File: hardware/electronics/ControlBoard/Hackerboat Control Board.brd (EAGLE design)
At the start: 177.8 x 114.3 mm, 52 parts, among them J3 3-1437664-0, U14 TPS54331, U15 TPS54331

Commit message: Everything in except the 15V boost converter and a couple of connectors
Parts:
- removed 5V/1-STAT: (no value), adafruit:CHIPLED_0805
- added 5V-STAT: (no value), adafruit:CHIPLED_0805
- added ACC_POWER: (no value), pinhead-1:2X08
- added BBB_CONSOLE: FTDI_BASICPTH, SparkFun-Connectors:FTDI_BASIC
- added C1, C2, C3, C4, C5, C6: (no value), resistor:C0603
- added C10, C11, C12, C13, C14, C15, C16, C35, C36, C37, C38, C39, C7, C8, C9: 100n, resistor:C0603
- added D1, D10, D11, D12, D13, D14, D15, D16, D17, D18, D19, D2, D3, D4, D5, D6, D7, D8, D9: (no value), adafruit:SOD-123
- added IC1: 74AHC1G08DBV, 74xx-little-us:SOT23-5
- added J1, J2: (no value), SparkFun-Connectors:1X03_LOCK
- added J4: (no value), SparkFun-Connectors:1X05_LOCK
- added J5: (no value), SparkFun-Connectors:1X09_LOCK
- added J6: (no value), SparkFun-Connectors:1X10_LOCK
- added J7: (no value), SparkFun-Connectors:1X18
- added MOTOR-CTRL-RELAYS: (no value), SparkFun-Connectors:DB9
- added POE-DEVICE, POE-LAN: RJ45, SparkFun-Connectors:RJ45-8
- added POWER_INPUT: 3-1437664-0, logos-headers:CONN-2
- added POWER_MONITOR: (no value), pinhead-1:2X06
- added POWER_STATE: HEADER_POS5_70555, con-molex-c-grid-sl:70555-POS5
- added R1, R13, R14, R15, R2, R25, R29, R3, R30, R34, R35, R36, R42, R43, R44, R48, R69, R7, R70, R71, R75, R76, R77, R8, R81, R82, R83, R9: 10K, resistor:R0603
- added R10, R16, R31, R37, R4, R45, R72, R78, R84: 100K, resistor:R0603
- added R11, R17, R32, R40, R46, R5, R55, R73, R79, R85: 0R05, resistor:R2512
- added R12, R18, R33, R41, R47, R56, R6, R74, R80, R86: 33K, resistor:R0603
- added R49, R50: (no value), resistor:R0603
- added R51, R52, R53, R54: 4u7, resistor:R0603
- added S1: FONA, adafruit-sensor-boards:FONA-3G
- added SERIAL_CONSOLE: HEADER_POS4_70555, con-molex-c-grid-sl:70555-POS4
- added STATUS_LIGHTS, STEERING: HEADER_POS3_70555, con-molex-c-grid-sl:70555-POS3
- added U1, U11, U2, U20, U22, U24, U4, U6, U8: IPS6041G, hackerbot:SO08
- added U10, U12, U21, U23, U25, U27, U3, U5, U7, U9: INA169, logos-power:SOT23-5L
- added U13, U16, U17: (no value), adafruit:TSSOP20
- added U18, U19: ADC128D818, ti-stuff:TSSOP16
- added U26: (no value), adafruit:VFSOP-8
- J3: value 3-1437664-0 -> (none); device logos-headers:CONN-2 -> SparkFun-Connectors:1X04_LOCK
- moved J3 501.0 mm to (19.7, -398.1), turned to 0 degrees
- moved C17 406.4 mm to (429.3, 31.8)
- moved C18 406.4 mm to (429.3, 28.6)
- moved C19 406.4 mm to (429.3, 26.0)
- moved C20 406.4 mm to (433.7, 25.4)
- moved C21 406.4 mm to (442.6, 35.6)
- moved C22 406.4 mm to (437.5, 25.4)
- moved C23 406.4 mm to (439.4, 25.4)
- moved C24 406.4 mm to (452.1, 22.2)
- moved C25 406.4 mm to (445.1, 22.2)
- moved D35 406.4 mm to (442.6, 30.5)
- moved L1 406.4 mm to (448.3, 30.5)
- moved R21 406.4 mm to (435.6, 25.4)
- moved R22 406.4 mm to (443.2, 25.4)
- moved R23 406.4 mm to (441.3, 25.4)
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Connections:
- net N$109 renamed BBB_MISO
- net N$168 renamed BBB_SCLK
- net N$169 renamed BBB_MOSI
- net RX1 renamed N$21
- net TX1 renamed BBB_STAT_LIGHT_3V3
- removed net 7V4: C26.1, C27.1, L2.2, R27.2, R39.2
- removed net N$105: U$1.86, U$2.6
- removed net N$111: U$1.66, U$2.16
- removed net N$112: U$1.64, U$2.17
- removed net N$113: U$1.62, U$2.18
- removed net N$114: U$1.60, U$2.19
- removed net N$115: U$1.58, U$2.20
- removed net N$116: U$1.56, U$2.21
- removed net N$122: U$1.40, U$3.5
- removed net N$123: U$1.38, U$3.6
- removed net N$124: U$1.36, U$3.7
- removed net N$125: U$1.34, U$3.8
- removed net N$126: U$1.32, U$3.9
- removed net N$127: U$1.30, U$3.10
- removed net N$128: U$1.28, U$3.11
- removed net N$129: U$1.26, U$3.12
- removed net N$130: U$1.24, U$3.13
- removed net N$131: U$1.22, U$3.14
- removed net N$132: U$1.20, U$3.15
- removed net N$133: U$1.18, U$3.16
- removed net N$134: U$1.16, U$3.17
- removed net N$135: U$1.14, U$3.18
- removed net N$136: U$1.12, U$3.19
- removed net N$137: U$1.10, U$3.20
- removed net N$138: U$1.8, U$3.21
- removed net N$139: U$1.6, U$3.22
- removed net N$140: U$1.4, U$3.23
- removed net N$145: U$1.37, U$4.6
- removed net N$147: U$1.33, U$4.8
- removed net N$148: U$1.31, U$4.9
- removed net N$149: U$1.29, U$4.10
- removed net N$150: U$1.27, U$4.11
- removed net N$151: U$1.25, U$4.12
- removed net N$152: U$1.23, U$4.13
- removed net N$153: U$1.21, U$4.14
- removed net N$154: U$1.19, U$4.15
- removed net N$155: U$1.17, U$4.16
- removed net N$156: U$1.15, U$4.17
- removed net N$157: U$1.13, U$4.18
- removed net N$158: U$1.11, U$4.19
- removed net N$159: U$1.9, U$4.20
- removed net N$160: U$1.7, U$4.21
- removed net N$161: U$1.5, U$4.22
- removed net N$162: U$1.3, U$4.23
- removed net N$173: U$1.65, U$5.16
- removed net N$174: U$1.63, U$5.17
- removed net N$175: U$1.61, U$5.18
- removed net N$196: IMU.SDA, R20.1
- removed net N$197: IMU.SCL, R19.1
- removed net RX0: U$1.70, U$2.14
- removed net SERVO_EN: U15.3
- removed net TX0: U$1.72, U$2.13
- new net +15V: ACC_POWER.13, ACC_POWER.14, POE-DEVICE.4, POE-DEVICE.5
- new net +7V4: ACC_POWER.15, ACC_POWER.16, J1.1, R55.2, STEERING.P$1, U27.4
- new net +7V4_OUT: C26.1, C27.1, L2.2, R27.2, R39.2, R55.1, U27.3
- new net AUX_ADC_0: POWER_MONITOR.10, U19.11
- new net AUX_ADC_1: POWER_MONITOR.11, U19.10
- new net AUX_GPIO_0_3V3: U$1.21, U$4.14, U16.9
- new net AUX_GPIO_0_5V: U16.12
- new net AUX_GPIO_1_3V3: U$1.23, U$4.13, U17.4
- new net AUX_GPIO_1_5V: U17.17
- new net AUX_GPIO_2_3V3: U$1.25, U$4.12, U17.5
- new net AUX_GPIO_2_5V: U17.16
- new net AUX_GPIO_3_3V3: U$1.27, U$4.11, U17.6
- new net AUX_GPIO_3_5V: U17.15
- new net AUX_GPIO_4_3V3: U$1.29, U$4.10, U17.7
- new net AUX_GPIO_4_5V: U17.14
- new net AUX_GPIO_5_3V3: U$1.33, U$4.8, U17.8
- new net AUX_GPIO_5_5V: U17.13
- new net BATMON: D13.C, R49.1, R50.2, U$1.86, U$2.6
- new net BBB_I2C_1_SCL: IMU.SCL, J6.4, R19.1, U$1.63, U$5.17
- new net BBB_I2C_1_SDA: IMU.SDA, J6.5, R20.1, U$1.64, U$2.17
- new net BBB_I2C_2_SCL: R53.1, U$1.65, U$5.16, U26.P$4
- new net BBB_I2C_2_SDA: R54.1, U$1.66, U$2.16, U26.P$5
- new net BBB_RESET_3V3: R48.2, U$1.56, U$2.21, U16.8
- new net BBB_RESET_5V: U16.13
- new net BBB_STATUS_LIGHTS_5V: J2.2, STATUS_LIGHTS.P$2
- new net BBB_STATUS_LIGHT_3V3: U16.7
- new net BBB_STATUS_LIGHT_5V: U16.14
- new net BBB_UART0_DTR: BBB_CONSOLE.DTR, J3.1, SERIAL_CONSOLE.P$1
- new net BBB_UART0_RX: BBB_CONSOLE.RXI, J3.2, SERIAL_CONSOLE.P$2
- new net BBB_UART0_TX: BBB_CONSOLE.TXO, J3.3, SERIAL_CONSOLE.P$3
- new net BBB_UART1_RX_3V3: U$1.70, U$2.14, U17.1
- new net BBB_UART1_RX_5V: U17.20
- new net BBB_UART1_TX_3V3: U$1.72, U$2.13, U17.3
- new net BBB_UART1_TX_5V: U17.18
- new net CELL_CTS: J7.9, S1.CTS, U$1.31, U$4.9
- new net CELL_KEY: J7.8, S1.KEY, U$1.40, U$3.5
- new net CELL_NET_STATUS: J7.5, S1.NS, U$1.34, U$3.8
- new net CELL_POWER_STATUS: J7.6, S1.PS, U$1.28, U$3.11
- new net CELL_RESET: J7.14, S1.RST, U$1.36, U$3.7
- new net CELL_RING: J7.7, S1.RI, U$1.30, U$3.10
- new net CELL_RTS: J7.11, S1.RTS, U$1.32, U$3.9
- new net CELL_RX: J7.13, S1.RX, U$1.37, U$4.6
- new net CELL_TX: J7.12, S1.TX, U$1.38, U$3.6
- new net CHARGE_CURRENT: POWER_MONITOR.7, U19.12
- new net CHARGE_VOLTAGE: POWER_MONITOR.6, U19.13
- new net DISARM_RELAY_IN_3V3: U$1.22, U$3.14, U16.6
- new net DISARM_RELAY_IN_5V: J4.2, POWER_STATE.P$2, U16.15
- new net ENABLE_RELAY_IN_3V3: U$1.20, U$3.15, U16.5
- new net ENABLE_RELAY_IN_5V: IC1.2, J4.1, POWER_STATE.P$1, U16.16
- new net GNSS_ENABLE: GPS.EN, J5.8, U$1.58, U$2.20
- new net GNSS_FIX: GPS.FIX, J5.6, U$1.61, U$5.18
- new net MOT_CURRENT: POWER_MONITOR.3, U19.15
- new net MOT_VOLTAGE: POWER_MONITOR.2, U19.14
- new net N$1: R1.2, R2.1, U1.3
- new net N$10: R25.2, R29.1, U6.3
- new net N$11: R30.2, U6.2
- new net N$12: R31.1, R32.1, U6.4, U7.3
- new net N$13: R34.2, R35.1, U8.3
- new net N$14: R36.2, U8.2
- new net N$15: R37.1, R40.1, U10.3, U8.4
- new net N$16: R42.2, R43.1, U11.3
- new net N$17: R44.2, U11.2
- new net N$18: R45.1, R46.1, U11.4, U12.3
- new net N$19: GPS.PPS, J5.1
- new net N$2: R3.2, U1.2
- new net N$20: GPS.VBAT, J5.7
- new net N$23: R52.1, U18.2, U19.2, U26.P$8
- new net N$24: R69.2, R70.1, U20.3
- new net N$25: R71.2, U20.2
- new net N$26: R72.1, R73.1, U20.4, U21.3
- new net N$27: R51.1, U18.3, U19.3, U26.P$1
- new net N$28: IMU.3VO, J6.2
- new net N$29: IMU.GINT, J6.6
- new net N$3: R4.1, R5.1, U1.4, U9.3
- new net N$30: IMU.GRDY, J6.7
- new net N$31: IMU.LIN1, J6.8
- new net N$32: IMU.LIN2, J6.9
- new net N$33: IMU.LRDY, J6.10
- new net N$34: R75.2, R76.1, U22.3
- new net N$35: GPS.3V3, J5.9
- new net N$36: IC1.4, U15.3
- new net N$37: J7.2, S1.SPKR+
- new net N$38: J7.3, S1.MIC-
- new net N$39: J7.4, S1.MIC+
- new net N$4: R7.2, R8.1, U2.3
- new net N$40: J7.10, S1.DTR
- new net N$41: J7.17, S1.BAT
- new net N$42: J7.1, S1.SPKR-
- new net N$43: POE-DEVICE.1, POE-LAN.1
- new net N$44: POE-DEVICE.2, POE-LAN.2
- new net N$45: POE-DEVICE.3, POE-LAN.3
- new net N$48: R77.2, U22.2
- new net N$49: R78.1, R79.1, U22.4, U23.3
- new net N$5: R9.2, U2.2
- new net N$50: R81.2, R82.1, U24.3
- new net N$51: R83.2, U24.2
- new net N$52: R84.1, R85.1, U24.4, U25.3
- new net N$54: POE-DEVICE.6, POE-LAN.6
- new net N$6: R10.1, R11.1, U2.4, U3.3
- new net N$7: R13.2, R14.1, U4.3
- new net N$8: R15.2, U4.2
- new net N$9: R16.1, R17.1, U4.4, U5.3
- new net RELAY_CURRENT_0: R6.2, U18.16, U9.1
- new net RELAY_CURRENT_1: R12.2, U18.15, U3.1
- new net RELAY_CURRENT_2: R18.2, U18.14, U5.1
- new net RELAY_CURRENT_3: R33.2, U18.13, U7.1
- new net RELAY_CURRENT_4: R41.2, U10.1, U18.12
- new net RELAY_CURRENT_5: R47.2, U12.1, U18.11
- new net RELAY_CURRENT_DISARM: R74.2, U18.10, U21.1
- new net RELAY_CURRENT_ENABLE: R86.2, U18.9, U25.1
- new net RELAY_CURRENT_HORN: R80.2, U19.16, U23.1
- new net RELAY_DISARM_3V3: U$1.15, U$4.17, U13.8
- new net RELAY_DISARM_5V: R71.1, U13.13
- new net RELAY_DISARM_FAULT: R69.1, U$1.16, U$3.17
- new net RELAY_ENABLE_3V3: U$1.24, U$3.13, U16.1
- new net RELAY_ENABLE_5V: R83.1, U16.20
- new net RELAY_ENABLE_FAULT: R81.1, U$1.26, U$3.12
- new net RELAY_FAULT_0: R1.1, U$1.4, U$3.23
- new net RELAY_FAULT_1: R7.1, U$1.6, U$3.22
- new net RELAY_FAULT_2: R13.1, U$1.8, U$3.21
- new net RELAY_FAULT_3: R25.1, U$1.10, U$3.20
- new net RELAY_FAULT_4: R34.1, U$1.12, U$3.19
- new net RELAY_FAULT_5: R42.1, U$1.14, U$3.18
- new net RELAY_HORN_3V3: U$1.17, U$4.16, U13.9
- new net RELAY_HORN_5V: R77.1, U13.12
- new net RELAY_HORN_FAULT: R75.1, U$1.18, U$3.16
- new net RELAY_IN_0_3V3: U$1.3, U$4.23, U13.1
- new net RELAY_IN_0_5V: R3.1, U13.20
- new net RELAY_IN_1_3V3: U$1.5, U$4.22, U13.3
- new net RELAY_IN_1_5V: R9.1, U13.18
- new net RELAY_IN_2_3V3: U$1.7, U$4.21, U13.4
- new net RELAY_IN_2_5V: R15.1, U13.17
- new net RELAY_IN_3_3V3: U$1.9, U$4.20, U13.5
- new net RELAY_IN_3_5V: R30.1, U13.16
- new net RELAY_IN_4_3V3: U$1.11, U$4.19, U13.6
- new net RELAY_IN_4_5V: R36.1, U13.15
- new net RELAY_IN_5_3V3: U$1.13, U$4.18, U13.7
- new net RELAY_IN_5_5V: R44.1, U13.14
- new net RELAY_OUT_0: D1.A, D2.C, MOTOR-CTRL-RELAYS.1, R5.2, U9.4
- new net RELAY_OUT_1: D3.A, D4.C, MOTOR-CTRL-RELAYS.3, R11.2, U3.4
- new net RELAY_OUT_2: D5.A, D6.C, MOTOR-CTRL-RELAYS.5, R17.2, U5.4
- new net RELAY_OUT_3: D11.A, D12.C, MOTOR-CTRL-RELAYS.6, R32.2, U7.4
- new net RELAY_OUT_4: D10.A, D9.C, MOTOR-CTRL-RELAYS.8, R40.2, U10.4
- new net RELAY_OUT_5: D7.C, D8.A, MOTOR-CTRL-RELAYS.9, R46.2, U12.4
- new net RELAY_OUT_DISARM: D14.A, D15.C, J4.4, POWER_STATE.P$4, R73.2, U21.4
- new net RELAY_OUT_ENABLE: D18.A, D19.C, J4.5, POWER_STATE.P$5, R85.2, U25.4
- new net RELAY_OUT_HORN: D16.A, D17.C, R79.2, U23.4
- new net RS_485_DIR_SELECT_3V3: U$1.60, U$2.19, U16.3
- new net RS_485_DIR_SELECT_5V: U16.18
- new net SERVO_CURRENT_MON: R56.2, U19.9, U27.1
- new net SERVO_ENABLE_3V3: U$1.19, U$4.15, U16.4
- new net SERVO_ENABLE_5V: IC1.1, U16.17
- new net SERVO_RUDDER_3V3: U$1.62, U$2.18, U17.9
- new net SERVO_RUDDER_5V: J1.2, STEERING.P$2, U17.12
- net +12V: now also D1.C, D10.C, D11.C, D14.C, D16.C, D18.C, D3.C, D5.C, D8.C, POWER_INPUT.2, R10.2, R16.2, R31.2, R37.2, R4.2, R45.2, R49.2, R72.2, R78.2, R84.2, U1.5, U1.6, U1.7, U1.8, U11.5, U11.6, U11.7, U11.8, U2.5, U2.6, U2.7, U2.8, U20.5, U20.6, U20.7, U20.8, U22.5, U22.6, U22.7, U22.8, U24.5, U24.6, U24.7, U24.8, U4.5, U4.6, U4.7, U4.8, U6.5, U6.6, U6.7, U6.8, U8.5, U8.6, U8.7, U8.8; no longer J3.1
- net +3V3: now also ACC_POWER.10, ACC_POWER.7, ACC_POWER.8, ACC_POWER.9, C1.1, C3.1, C5.1, C8.2, J7.15, R14.2, R2.2, R29.2, R35.2, R43.2, R48.1, R53.2, R54.2, R70.2, R76.2, R8.2, R82.2, S1.VIO, U13.10, U13.2, U16.10, U16.2, U17.10, U17.2, U26.P$3, U26.P$6
- net +5V: now also ACC_POWER.1, ACC_POWER.2, ACC_POWER.3, ACC_POWER.4, C10.1, C11.1, C12.1, C13.2, C14.2, C15.2, C16.2, C2.1, C35.2, C36.2, C37.2, C38.2, C39.2, C4.1, C6.1, C7.1, C9.1, GPS.VIN, IC1.5, J2.1, J5.2, J6.1, J7.18, POWER_MONITOR.1, POWER_MONITOR.5, POWER_MONITOR.9, R51.2, R52.2, S1.5V, STATUS_LIGHTS.P$1, U10.5, U12.5, U13.19, U16.19, U17.19, U18.1, U18.5, U18.7, U19.1, U19.5, U21.5, U23.5, U25.5, U26.P$7, U27.5, U3.5, U5.5, U7.5, U9.5
- net GND: now also 5V-STAT.C, ACC_POWER.11, ACC_POWER.12, ACC_POWER.5, ACC_POWER.6, BBB_CONSOLE.GND, C1.2, C10.2, C11.2, C12.2, C13.1, C14.1, C15.1, C16.1, C2.2, C3.2, C35.1, C36.1, C37.1, C38.1, C39.1, C4.2, C5.2, C6.2, C7.2, C8.1, C9.2, D12.A, D13.A, D15.A, D17.A, D19.A, D2.A, D4.A, D6.A, D7.A, D9.A, GPS.GND, IC1.3, J1.3, J2.3, J3.4, J4.3, J5.3, J6.3, J7.16, MOTOR-CTRL-RELAYS.2, MOTOR-CTRL-RELAYS.4, MOTOR-CTRL-RELAYS.7, POE-DEVICE.7, POE-DEVICE.8, POWER_INPUT.1, POWER_MONITOR.12, POWER_MONITOR.4, POWER_MONITOR.8, POWER_STATE.P$3, R12.1, R18.1, R33.1, R41.1, R47.1, R50.1, R56.1, R6.1, R74.1, R80.1, R86.1, S1.GND, S1.P$1, S1.P$2, SERIAL_CONSOLE.P$4, STATUS_LIGHTS.P$3, STEERING.P$3, U$2.2, U$3.25, U$4.25, U$5.2, U1.1, U10.2, U11.1, U12.2, U13.11, U16.11, U17.11, U18.4, U18.8, U19.4, U19.7, U19.8, U2.1, U20.1, U21.2, U22.1, U23.2, U24.1, U25.2, U26.P$2, U27.2, U3.2, U4.1, U5.2, U6.1, U7.2, U8.1, U9.2; no longer 5V/1-STAT.C, J3.2
- net GNSS_RX: now also GPS.RX, J5.4
- net GNSS_TX: now also GPS.TX, J5.5
- net N$182: now also 5V-STAT.A; no longer 5V/1-STAT.A
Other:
- board outline removed

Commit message: All placed and routed for the control board.
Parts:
- removed H2: MOUNT-PAD-ROUND3.2, holes:3,2-PAD
- added AUX_GPIO: 2X6 FEMALE, SparkFun-Connectors:2X6
- added BBB_RESET, RS485: HEADER_POS3_70555, con-molex-c-grid-sl:70555-POS3
- added C40, C41, C42, C47, C48: 100n, resistor:C0603
- added C43, C44: 4u7, resistor:C1210
- added C45: 47n, resistor:C0603
- added C46: 68n, resistor:C0603
- added D20: (no value), ARD-SRG-MOT8-1a:SPARKFUN_SMA-DIODE
- added HORN: HEADER_POS2_70555, con-molex-c-grid-sl:70555-POS2
- added IC2: TINY861L-20SU, atmel:SO20L
- added IC3: 74AHC1G04DBV, 74xx-little-us:SOT23-5
- added J10, J11: (no value), SparkFun-Connectors:1X03_LOCK
- added J8: AVR_SPI_PRG_6PTH, SparkFun-Connectors:2X3
- added J9: (no value), SparkFun-Connectors:1X02_LOCK
- added L3: 22u, logos-inductors:SRN8040
- added R57: 10K, resistor:R0603
- added R58: 174K, resistor:R0603
- added R59: 1K62, resistor:R0603
- added R60: 182K, resistor:R0603
- added R61: 16K2, resistor:R0603
- added RC-IN-0, RC-IN-1, RC-IN-2, RC-IN-3, RC-IN-4, RC-IN-5, RC-IN-6, RC-IN-7: (no value), pinhead-1:1X03
- added U$6: RS485SOIC, SparkFun-DigitalIC:SO08
- added U28: (no value), adafruit:TSSOP20
- added U29: TPS61175, logos-power:HTSSOP14
- C1, C2, C3, C4, C5, C6: value (none) -> 100n
- C17, C18, C28, C29: value 4u7 -> 10u
- C20, C31: value 2n -> 8n2
- C22: value (none) -> 2n4
- C23: value (none) -> 56p
- C24, C25: value (none) -> 22u
- C26, C27: value (none) -> 4u7
- C33: value (none) -> 7u5
- C34: value (none) -> 220p
- D13: value (none) -> 1V8
- L1: value NR6045 -> 10u
- L2: value NR6045 -> 22u
- R21: value (none) -> 26K7
- R22, R27: value (none) -> 10K2
- R23: value (none) -> 1K96
- R24, R38, R39: value (none) -> 1K
- R26: value (none) -> 11K5
- R28: value (none) -> 1K24
- moved ACC_POWER 1014.6 mm to (111.8, 168.9), turned to 270 degrees
- moved C38 1004.2 mm to (109.2, 181.0), turned to 90 degrees
- moved C39 1001.4 mm to (59.7, 181.0), turned to 90 degrees
- moved C37 995.8 mm to (89.5, 181.0), turned to 90 degrees
- moved C36 989.4 mm to (20.3, 188.6), flipped to the bottom, turned to 180 degrees
- moved C35 985.5 mm to (31.8, 188.6), flipped to the bottom, turned to 180 degrees
- moved C16 981.1 mm to (48.3, 187.3), flipped to the bottom
- moved C15 976.0 mm to (37.5, 188.6), flipped to the bottom, turned to 180 degrees
- moved C14 969.7 mm to (26.0, 188.6), flipped to the bottom, turned to 180 degrees
- moved C13 963.7 mm to (9.53, 189.2), turned to 180 degrees
- moved C11 902.1 mm to (90.2, 135.3), turned to 180 degrees
- moved C12 899.5 mm to (109.2, 123.8), turned to 180 degrees
- moved R56 894.2 mm to (109.2, 130.2), turned to 180 degrees
- moved IC1 892.5 mm to (90.2, 132.7), turned to 270 degrees
- moved R55 886.5 mm to (104.1, 130.2), turned to 270 degrees
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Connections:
- removed net BBB_STATUS_LIGHT_5V: U16.14
- removed net N$144: U$1.39, U$4.5
- removed net N$146: U$1.35, U$4.7
- new net I2C_SCL_5V: AUX_GPIO.4, R51.1, U18.3, U19.3, U26.P$1
- new net I2C_SDA_5V: AUX_GPIO.3, R52.1, U18.2, U19.2, U26.P$8
- new net N$46: IC2.11, U28.9
- new net N$47: IC2.12, U28.8
- new net N$53: IC2.13, U28.7
- new net N$55: IC2.14, U28.6
- new net N$56: IC2.17, U28.5
- new net N$57: IC2.18, U28.4
- new net N$58: IC2.19, U28.3
- new net N$59: IC2.20, U28.1
- new net N$60: RC-IN-7.1, U28.12
- new net N$61: RC-IN-6.1, U28.13
- new net N$64: RC-IN-5.1, U28.14
- new net N$65: RC-IN-4.1, U28.15
- new net N$66: RC-IN-3.1, U28.16
- new net N$67: RC-IN-2.1, U28.17
- new net N$71: RC-IN-1.1, U28.18
- new net N$74: RC-IN-0.1, U28.20
- new net N$75: C46.1, R59.1
- new net N$76: R59.2, U29.8
- new net N$77: C45.1, U29.5
- new net N$83: R58.2, U29.10
- new net N$84: D20.A, L3.2, U29.1, U29.2
- new net N$85: R60.1, R61.2, U29.9
- new net N$86: J11.2, RS485.P$2, U$6.6
- new net RC_MODE_SELECT: IC2.9, R57.1, U$1.35, U$4.7
- new net RC_RESET: IC2.10, J8.5, U$1.39, U$4.5
- net +12V: now also C43.1, L3.1, U29.3, U29.4
- net +15V: now also C44.1, D20.C, R60.2
- net +3V3: now also C40.1, C41.1, IC2.15, IC2.5, J8.2, U28.10, U28.2
- net +5V: now also AUX_GPIO.1, AUX_GPIO.2, BBB_RESET.P$1, C42.1, C47.1, C48.1, IC3.5, J10.1, U$6.8, U28.19
- net +7V4: now also R39.2
- net +7V4_OUT: no longer R39.2
- net AUX_GPIO_0_3V3: now also U17.3; no longer U16.9
- net AUX_GPIO_0_5V: now also AUX_GPIO.5, U17.18; no longer U16.12
- net AUX_GPIO_1_3V3: now also U17.1; no longer U17.4
- net AUX_GPIO_1_5V: now also AUX_GPIO.6, U17.20; no longer U17.17
- net AUX_GPIO_2_5V: now also AUX_GPIO.7
- net AUX_GPIO_3_3V3: now also U17.4; no longer U17.6
- net AUX_GPIO_3_5V: now also AUX_GPIO.8, U17.17; no longer U17.15
- net AUX_GPIO_4_5V: now also AUX_GPIO.9
- net AUX_GPIO_5_3V3: now also U17.6; no longer U17.8
- net AUX_GPIO_5_5V: now also AUX_GPIO.10, U17.15; no longer U17.13
- net BBB_MISO: now also IC2.2, J8.1
- net BBB_MOSI: now also IC2.1, J8.4
- net BBB_RESET_5V: now also IC3.4
- net BBB_SCLK: now also IC2.3, J8.3
- net BBB_STATUS_LIGHTS_5V: now also U16.14
- net BBB_UART1_RX_3V3: now also U17.8; no longer U17.1
- net BBB_UART1_RX_5V: now also U$6.1, U17.13; no longer U17.20
- net BBB_UART1_TX_3V3: now also U17.9; no longer U17.3
- net BBB_UART1_TX_5V: now also U$6.4, U17.12; no longer U17.18
- net GND: now also AUX_GPIO.11, AUX_GPIO.12, BBB_RESET.P$3, C22.2, C33.2, C40.2, C41.2, C42.2, C43.2, C44.2, C45.2, C46.2, C47.2, C48.2, HORN.P$2, IC2.16, IC2.6, IC3.3, J10.3, J11.3, J8.6, J9.2, R57.2, R58.1, R61.1, RC-IN-0.3, RC-IN-1.3, RC-IN-2.3, RC-IN-3.3, RC-IN-4.3, RC-IN-5.3, RC-IN-6.3, RC-IN-7.3, RS485.P$3, U$6.5, U28.11, U29.11, U29.12, U29.13, U29.14, U29.6, U29.7, U29.P$1; no longer H2.B3,2, R21.1, R26.1
- net N$23: now also BBB_RESET.P$2, IC3.2, J10.2; no longer R52.1, U18.2, U19.2, U26.P$8
- net N$27: now also J11.1, RS485.P$1, U$6.7; no longer R51.1, U18.3, U19.3, U26.P$1
- net N$68: now also C22.1, R21.1; no longer C22.2, R21.2
- net N$70: now also R21.2; no longer C22.1
- net N$80: now also C33.1, R26.1; no longer C33.2, R26.2
- net N$81: now also R26.2; no longer C33.1
- net RELAY_OUT_HORN: now also HORN.P$1, J9.1
- net RS_485_DIR_SELECT_5V: now also U$6.2, U$6.3
- net SERVO_RUDDER_3V3: now also U16.9; no longer U17.9
- net SERVO_RUDDER_5V: now also U16.12; no longer U17.12
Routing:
- net +5V: track 0.00 -> 865.5 mm, vias 0 -> 38
- net +3V3: track 0.00 -> 652.9 mm, vias 0 -> 25
- net +12V: track 0.00 -> 357.1 mm, vias 0 -> 20
- net RELAY_DISARM_FAULT: track 0.00 -> 238.3 mm, vias 0 -> 6
- net +15V: track 0.00 -> 227.7 mm, vias 0 -> 4
- net RELAY_ENABLE_FAULT: track 0.00 -> 222.4 mm, vias 0 -> 5
- net BATMON: track 0.00 -> 210.3 mm, vias 0 -> 8
- net BBB_RESET_3V3: track 0.00 -> 207.5 mm, vias 0 -> 4
- net SERVO_ENABLE_3V3: track 0.00 -> 200.3 mm, vias 0 -> 6
- net RS_485_DIR_SELECT_3V3: track 0.00 -> 199.7 mm, vias 0 -> 4
- net ENABLE_RELAY_IN_3V3: track 0.00 -> 195.8 mm, vias 0 -> 4
- net BBB_I2C_2_SCL: track 0.00 -> 195.4 mm, vias 0 -> 8
- net RELAY_ENABLE_3V3: track 0.00 -> 193.8 mm, vias 0 -> 4
- net RELAY_FAULT_2: track 0.00 -> 193.2 mm, vias 0 -> 4
- net SERVO_RUDDER_3V3: track 0.00 -> 193.0 mm, vias 0 -> 4
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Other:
- board outline added: 114.3 x 209.6 mm

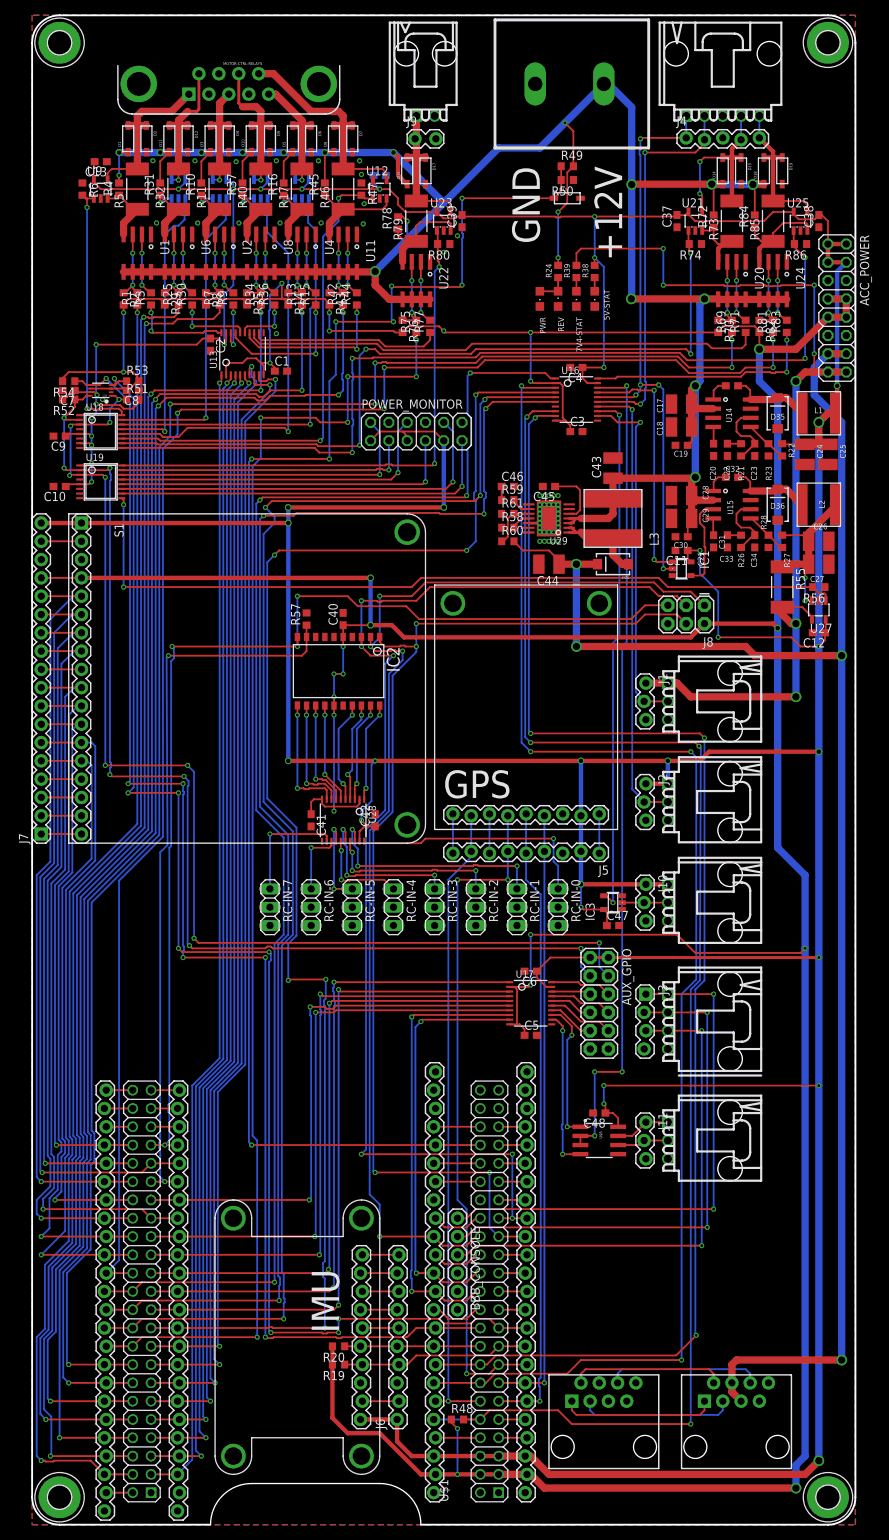
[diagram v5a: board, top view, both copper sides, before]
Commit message: Changed the R/C input over to SBUS. Updates to the PowerDistributionBaord
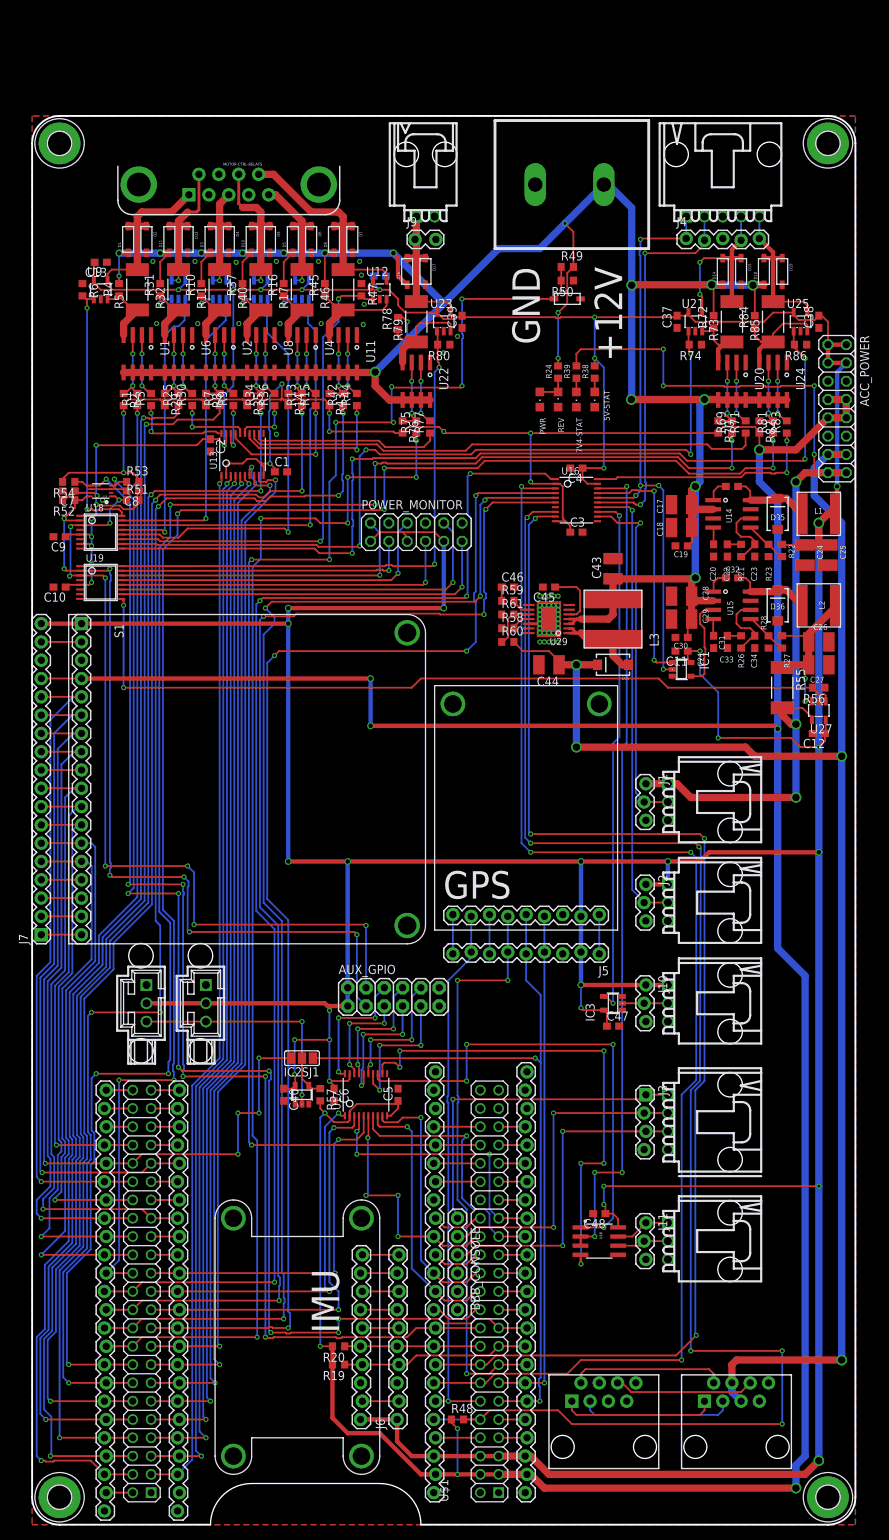
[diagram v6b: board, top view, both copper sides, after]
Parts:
- removed C41, C42: 100n, resistor:C0603
- removed J8: AVR_SPI_PRG_6PTH, SparkFun-Connectors:2X3
- removed RC-IN-0, RC-IN-1, RC-IN-2, RC-IN-3, RC-IN-4, RC-IN-5, RC-IN-6, RC-IN-7: (no value), pinhead-1:1X03
- removed U28: (no value), adafruit:TSSOP20
- added SBUS-IN, SBUS-OUT: HEADER_POS3_70545, con-molex-c-grid-sl:70545-POS3
- added SJ1: (no value), jumper:SJ_2
- C40: value 100n -> (none)
- IC2: value TINY861L-20SU -> 74AUC1G06DBV; device atmel:SO20L -> 74xx-little-us:SOT23-5
- R57: value 10K -> (none)
- moved C40 66.6 mm to (34.9, 59.7), turned to 270 degrees
- moved R57 66.1 mm to (40.0, 59.7), turned to 270 degrees
- moved IC2 58.7 mm to (37.5, 59.7), turned to 0 degrees
- moved AUX_GPIO 34.3 mm to (43.8, 72.0), turned to 0 degrees
- moved C6 32.2 mm to (41.9, 59.7), turned to 270 degrees
- moved U17 26.2 mm to (46.4, 59.7), turned to 0 degrees
- moved C5 20.2 mm to (50.8, 59.7), turned to 90 degrees
- moved C19 14.0 mm to (90.2, 135.9)
- moved R55 14.0 mm to (104.1, 116.2)
- moved R56 14.0 mm to (109.2, 116.2)
- moved R58 14.0 mm to (66.0, 124.5)
- moved R61 14.0 mm to (66.0, 126.4)
- moved S1 14.0 mm to (5.08, 126.4)
- moved J11 14.0 mm to (85.1, 41.9)
- moved RS485 14.0 mm to (88.3, 39.4)
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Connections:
- net AUX_GPIO_3_5V renamed BBB_SCLK_5V
- net AUX_GPIO_4_5V renamed BBB_MOSI_5V
- net AUX_GPIO_5_5V renamed BBB_MISO_5V
- removed net AUX_GPIO_3_3V3: U$1.27, U$4.11, U17.4
- removed net AUX_GPIO_4_3V3: U$1.29, U$4.10, U17.7
- removed net AUX_GPIO_5_3V3: U$1.33, U$4.8, U17.6
- removed net N$59: IC2.20, U28.1
- removed net N$60: RC-IN-7.1, U28.12
- removed net N$61: RC-IN-6.1, U28.13
- removed net N$64: RC-IN-5.1, U28.14
- removed net N$65: RC-IN-4.1, U28.15
- removed net N$66: RC-IN-3.1, U28.16
- removed net N$67: RC-IN-2.1, U28.17
- removed net N$71: RC-IN-1.1, U28.18
- removed net N$74: RC-IN-0.1, U28.20
- removed net RC_MODE_SELECT: IC2.9, R57.1, U$1.35, U$4.7
- removed net RC_RESET: IC2.10, J8.5, U$1.39, U$4.5
- net +3V3: now also R57.2; no longer C40.1, C41.1, IC2.15, IC2.5, J8.2, U28.10, U28.2
- net +5V: now also C40.1, IC2.5, SBUS-IN.P$2, SBUS-OUT.P$2; no longer C42.1, U28.19
- net BBB_MISO: now also U17.6; no longer IC2.2, J8.1
- net BBB_MOSI: now also U17.7; no longer IC2.1, J8.4
- net BBB_SCLK: now also U17.4; no longer IC2.3, J8.3
- net CELL_TX: now also SJ1.3
- net GND: now also IC2.3, SBUS-IN.P$1, SBUS-OUT.P$1; no longer C41.2, C42.2, IC2.16, IC2.6, J8.6, R57.2, RC-IN-0.3, RC-IN-1.3, RC-IN-2.3, RC-IN-3.3, RC-IN-4.3, RC-IN-5.3, RC-IN-6.3, RC-IN-7.3, U28.11
- net GNSS_TX: now also SJ1.1
- net N$46: now also U$1.27, U$4.11; no longer IC2.11, U28.9
- net N$47: now also U$1.29, U$4.10; no longer IC2.12, U28.8
- net N$53: now also IC2.2, SBUS-IN.P$3, SBUS-OUT.P$3; no longer IC2.13, U28.7
- net N$55: now also IC2.4, R57.1, SJ1.2; no longer IC2.14, U28.6
- net N$56: now also U$1.33, U$4.8; no longer IC2.17, U28.5
- net N$57: now also U$1.35, U$4.7; no longer IC2.18, U28.4
- net N$58: now also U$1.39, U$4.5; no longer IC2.19, U28.3
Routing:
- net RC_RESET: track 152.9 -> 0.00 mm, vias 4 -> 0
- net BBB_SCLK: track 164.5 -> 37.2 mm, vias 6 -> 3
- net BBB_MISO: track 159.6 -> 33.8 mm
- net BBB_MOSI: track 152.4 -> 36.2 mm, vias 4 -> 1
- net RC_MODE_SELECT: track 100.6 -> 0.00 mm, vias 2 -> 0
- net AUX_GPIO_3_3V3: track 86.1 -> 0.00 mm, vias 2 -> 0
- net AUX_GPIO_4_3V3: track 80.9 -> 0.00 mm, vias 2 -> 0
- net AUX_GPIO_5_3V3: track 76.9 -> 0.00 mm, vias 2 -> 0
- net +3V3: track 652.9 -> 589.0 mm, vias 25 -> 18
- net BBB_UART1_RX_5V: track 19.5 -> 67.8 mm, vias 2 -> 4
- net BBB_UART1_TX_5V: track 22.2 -> 68.7 mm, vias 2 -> 6
- net I2C_SCL_5V: track 161.2 -> 116.3 mm
- net I2C_SDA_5V: track 157.5 -> 116.4 mm
- net AUX_GPIO_1_3V3: track 92.6 -> 51.6 mm
- net AUX_GPIO_0_3V3: track 94.0 -> 56.4 mm
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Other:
- board size 114.3 x 209.6 mm -> 114.3 x 195.6 mm
